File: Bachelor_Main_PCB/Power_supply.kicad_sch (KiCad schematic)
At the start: 44 parts, among them IC1 LD3985M18R, J22 691137710002, U10 LMR51450FNDRRR, U11 LMR51450FNDRRR, U9 LM73100RPWR

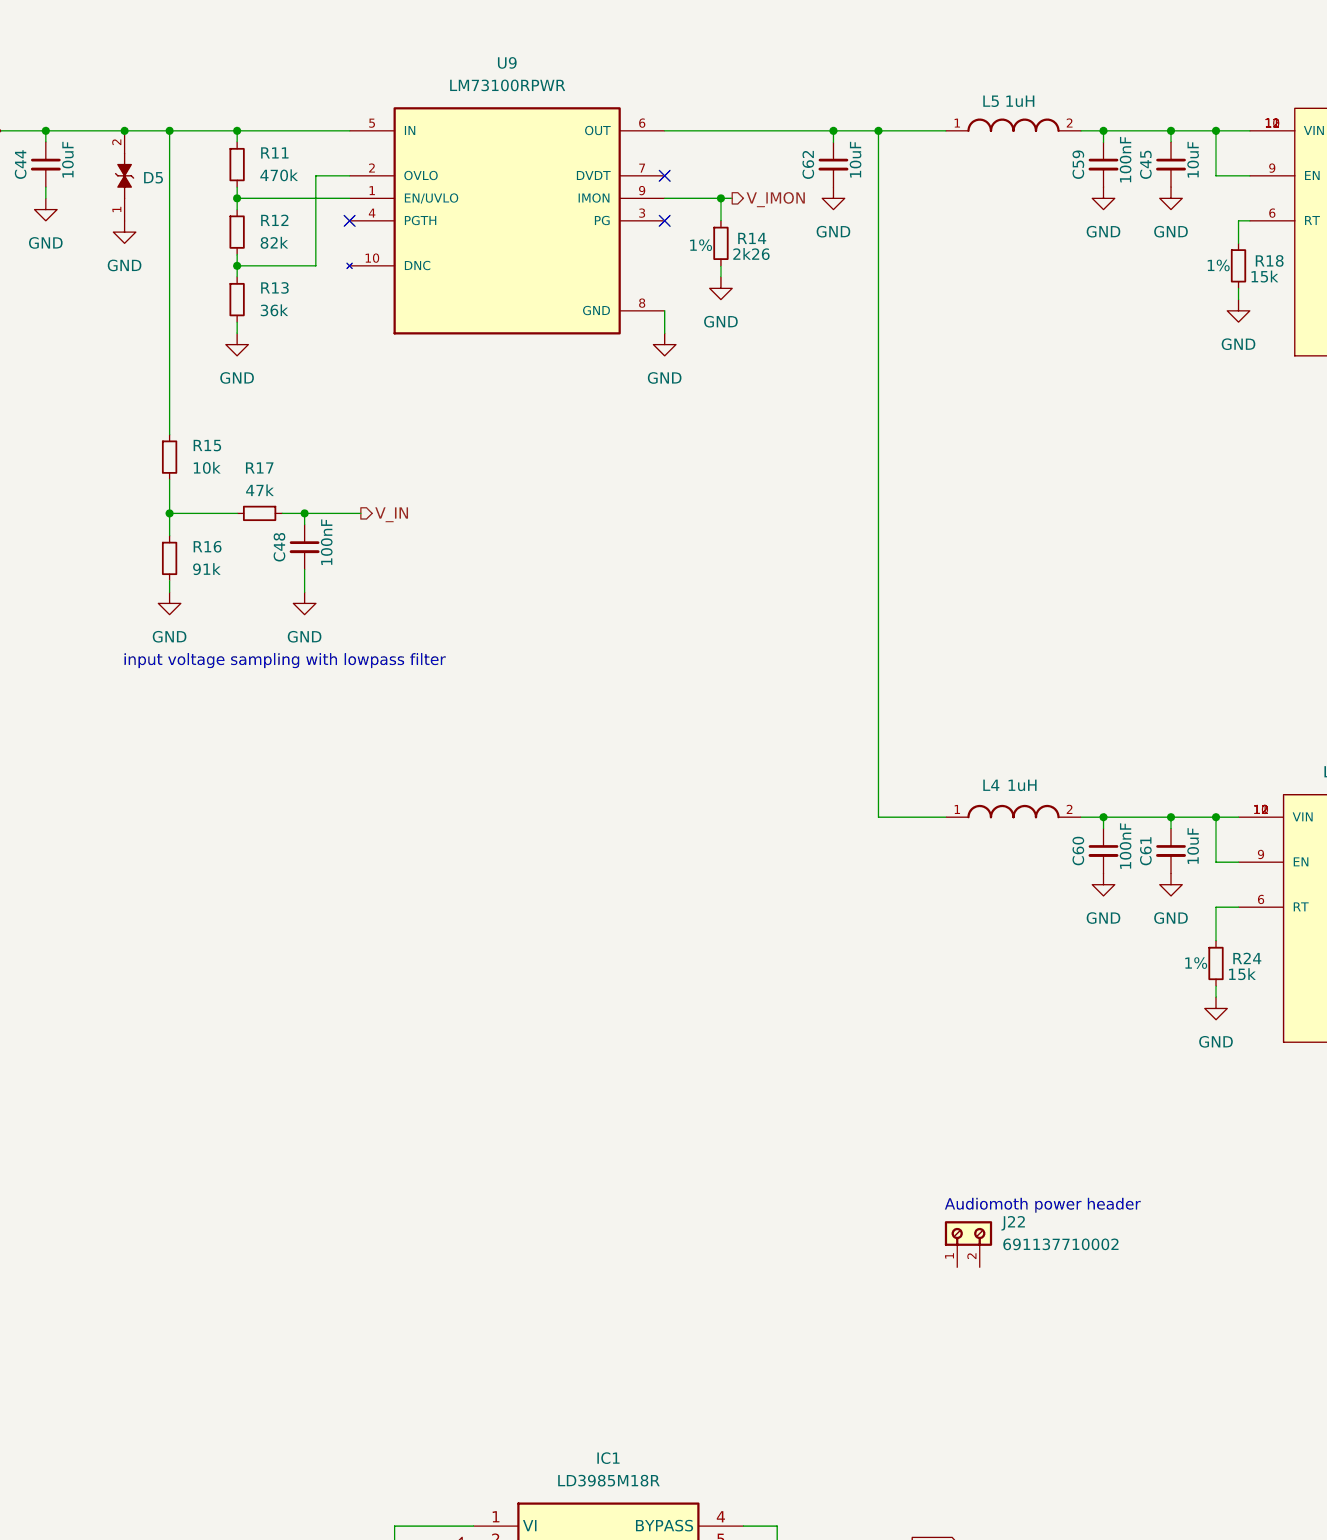
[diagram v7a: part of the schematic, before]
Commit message: Add BC817 and complete capacitance multiplier
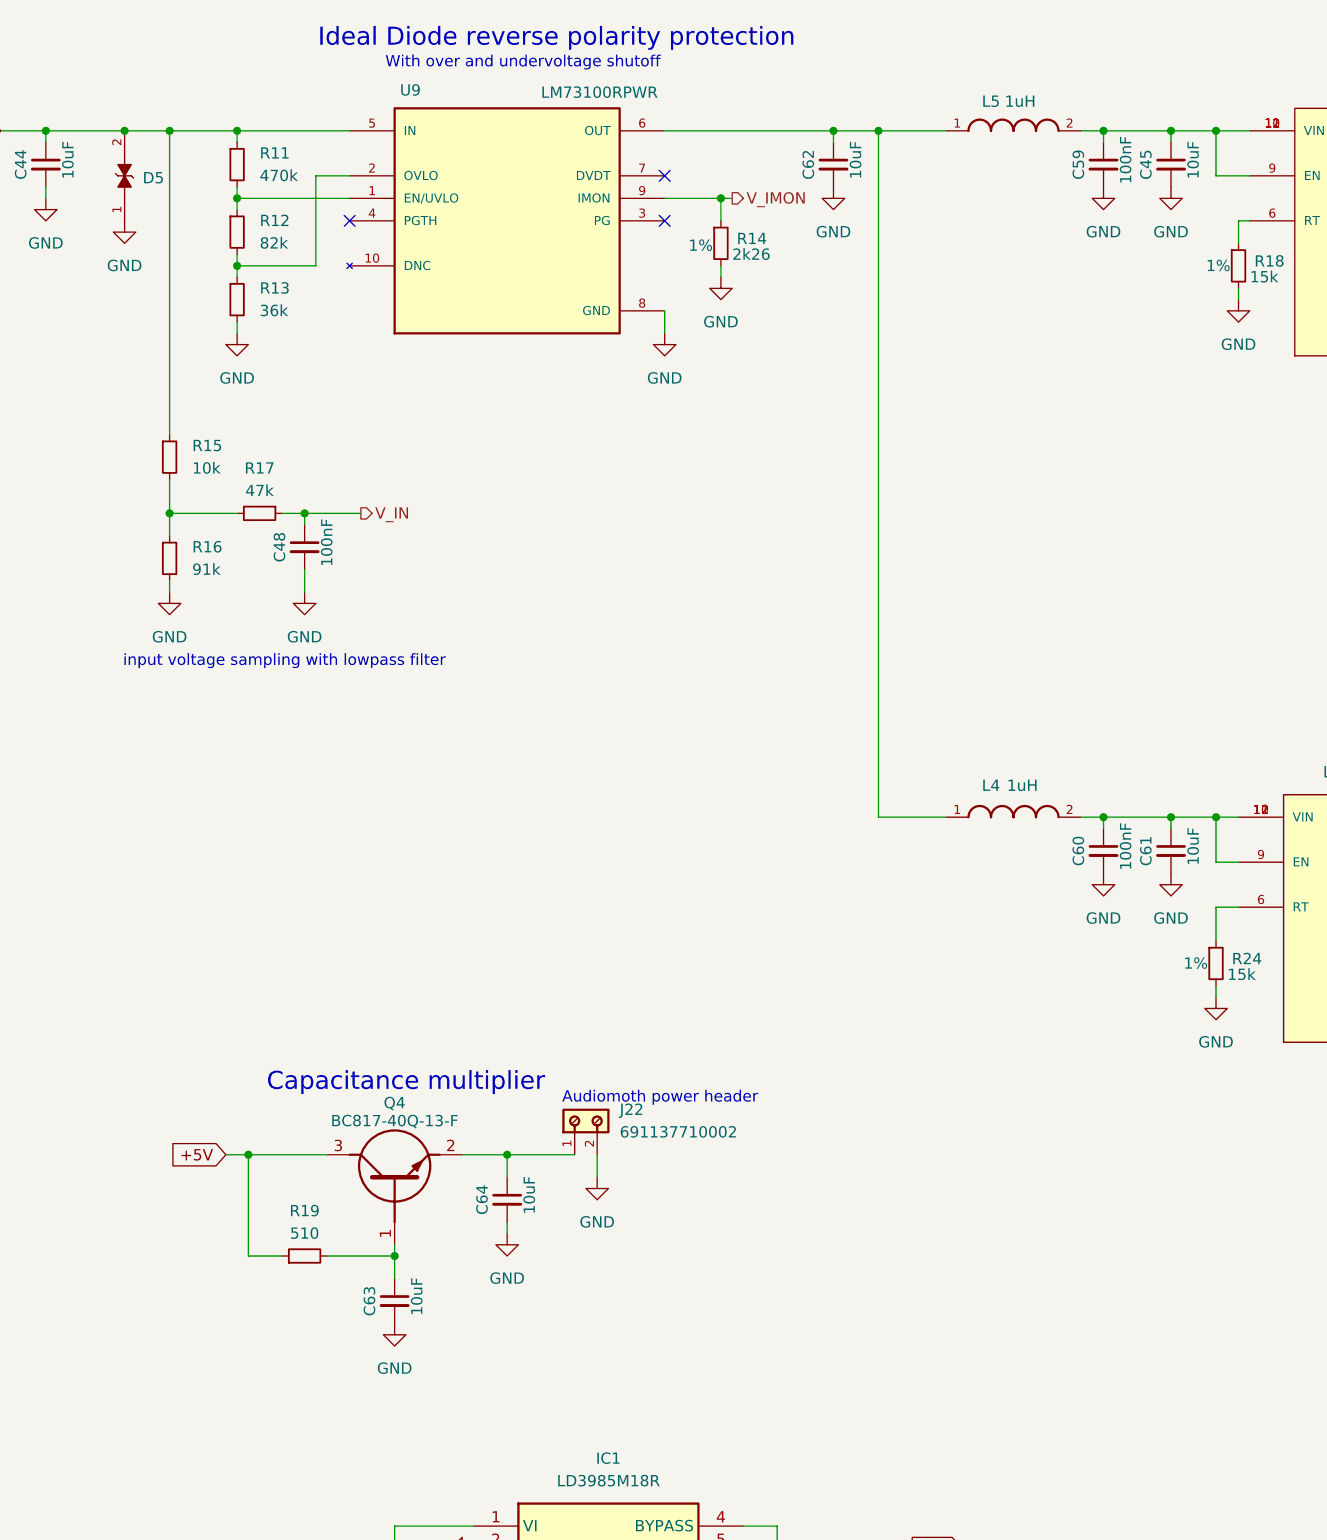
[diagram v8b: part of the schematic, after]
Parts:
- added C63, C64: 10uF, Capacitor_SMD:C_0603_1608Metric, symbol Device:C_Small
- added Q4: BC817-40Q-13-F, SOT96P240X110-3N, symbol BC817-40Q-13-F:BC817-40Q-13-F
- added R19: 510, Resistor_SMD:R_0402_1005Metric, symbol Device:R_Small
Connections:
- net +5V: now also Q4.3 (C), R19.1
- net GND: now also J22.2, C63.2, C64.2
- net at J22.1: now also C64.1, Q4.2 (E)
- new net: C63.1, Q4.1 (B), R19.2
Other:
- note added: "Capacitance multiplier"
- note added: "Ideal Diode reverse polarity protection"
- note added: "With over and undervoltage shutoff"
- moved on the sheet: J22
